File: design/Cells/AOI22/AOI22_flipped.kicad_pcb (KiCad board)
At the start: 2 copper layers, 8 parts, among them P1 Q_PJFET_GSD, P2 Q_PJFET_GSD, P3 Q_PJFET_GSD, P4 Q_PJFET_GSD

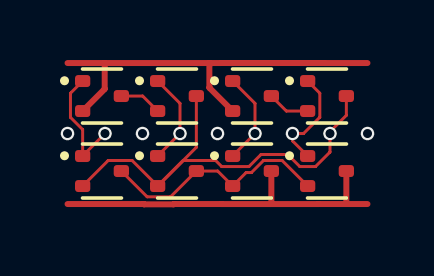
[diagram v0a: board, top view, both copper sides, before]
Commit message: All gates layout on a strict 2.5mm grid. Flipped versions of all three layouts
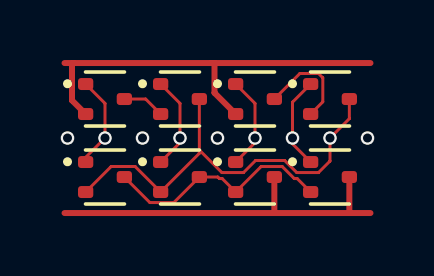
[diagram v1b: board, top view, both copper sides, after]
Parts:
- moved P1 0.22 mm to (1.25, 3.80)
- moved P2 0.22 mm to (3.75, 3.80)
- moved P3 0.22 mm to (6.25, 3.80)
- moved P4 0.22 mm to (8.75, 3.80)
- moved N1 0.14 mm to (1.25, 1.20)
- moved N2 0.14 mm to (3.75, 1.20)
- moved N3 0.14 mm to (6.25, 1.20)
- moved N4 0.14 mm to (8.75, 1.20)
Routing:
- net Net-(N3-D): track 1.42 -> 3.40 mm
- net Y: track 15.5 -> 14.3 mm
- net A: track 3.89 -> 3.13 mm

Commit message: flip the cells to share power lines
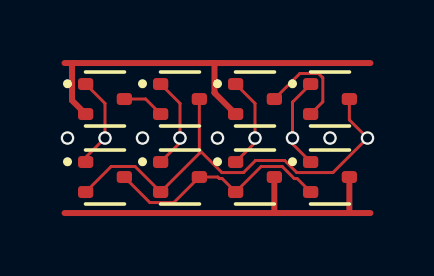
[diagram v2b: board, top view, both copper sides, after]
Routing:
- net Y: track 14.3 -> 15.1 mm
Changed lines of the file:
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@@
-	)
-	(via
-		(at 10 2.5)
-		(size 0.45)
-		(drill 0.3)
-		(layers "F.Cu" "B.Cu")
-		(net 0)
 	)
 	(via
@@
 	(via
 		(at 0 2.5)
+		(size 0.45)
+		(drill 0.3)
+		(layers "F.Cu" "B.Cu")
+		(net 0)
+	)
+	(via
+		(at 8.75 2.5)
 		(size 0.45)
 		(drill 0.3)
@@
 	)
 	(segment
-		(start 8.366738 3.651)
-		(end 7.64158 3.651)
-		(width 0.1)
-		(layer "F.Cu")
-		(net 5)
-	)
-	(segment
-		(start 8.75 2.5)
-		(end 8.75 3.267738)
-		(width 0.1)
-		(layer "F.Cu")
-		(net 5)
-	)
-	(segment
-		(start 9.395 1.855)
-		(end 8.75 2.5)
-		(width 0.1)
-		(layer "F.Cu")
-		(net 5)
-	)
-	(segment
-		(start 5.146 3.651)
-		(end 4.395 2.9)
-		(width 0.1)
-		(layer "F.Cu")
-		(net 5)
-	)
-	(segment
 		(start 1.456 3.449)
 		(end 0.605 4.3)
@@
 	)
 	(segment
-		(start 5.866738 3.651)
-		(end 5.146 3.651)
-		(width 0.1)
-		(layer "F.Cu")
-		(net 5)
-	)
-	(segment
 		(start 3.105 4.3)
 		(end 4.395 3.01)
@@
 	)
 	(segment
-		(start 8.75 3.267738)
-		(end 8.366738 3.651)
+		(start 6.268738 3.249)
+		(end 7.239581 3.249)
+		(width 0.1)
+		(layer "F.Cu")
+		(net 5)
+	)
+	(segment
+		(start 4.395 2.9)
+		(end 5.146 3.651)
+		(width 0.1)
+		(layer "F.Cu")
+		(net 5)
+	)
+	(segment
+		(start 9.395 1.895)
+		(end 9.395 1.2)
+		(width 0.1)
+		(layer "F.Cu")
+		(net 5)
+	)
+	(segment
+		(start 10 2.5)
+		(end 9.395 1.895)
 		(width 0.1)
 		(layer "F.Cu")
@@
 	)
 	(segment
+		(start 8.849 3.651)
+		(end 10 2.5)
+		(width 0.1)
+		(layer "F.Cu")
+		(net 5)
+	)
+	(segment
+		(start 7.239581 3.249)
+		(end 7.64158 3.651)
+		(width 0.1)
+		(layer "F.Cu")
+		(net 5)
+	)
+	(segment
 		(start 3.105 4.3)
 		(end 2.254 3.449)
@@
 	)
 	(segment
-		(start 7.239581 3.249)
+		(start 7.64158 3.651)
+		(end 8.849 3.651)
+		(width 0.1)
+		(layer "F.Cu")
+		(net 5)
+	)
+	(segment
+		(start 5.146 3.651)
+		(end 5.866738 3.651)
+		(width 0.1)
+		(layer "F.Cu")
+		(net 5)
+	)
+	(segment
+		(start 5.866738 3.651)
 		(end 6.268738 3.249)
 		(width 0.1)
@@
 		(net 5)
 	)
-	(segment
-		(start 7.64158 3.651)
-		(end 7.239581 3.249)
-		(width 0.1)
-		(layer "F.Cu")
-		(net 5)
-	)
-	(segment
-		(start 9.395 1.2)
-		(end 9.395 1.855)
-		(width 0.1)
-		(layer "F.Cu")
-		(net 5)
-	)
-	(segment
-		(start 6.268738 3.249)
-		(end 5.866738 3.651)
-		(width 0.1)
-		(layer "F.Cu")
-		(net 5)
-	)
-	(via
-		(at 8.75 2.5)
-		(size 0.45)
-		(drill 0.3)
+	(via
+		(at 10 2.5)
+		(size 0.45)
+		(drill 0.3)
